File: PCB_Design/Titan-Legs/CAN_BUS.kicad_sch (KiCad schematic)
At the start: 4 parts, among them P2 282837-2, U3 SN65HVD230DR

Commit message: Added high voltage copper fills
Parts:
- R13: footprint Resistor_SMD:R_0603_1608Metric -> Resistor_SMD:R_0402_1005Metric
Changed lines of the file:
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@@
       (effects (font (size 1 1)) (justify left))
     )
-    (property "Footprint" "Resistor_SMD:R_0603_1608Metric" (id 2) (at 108.712 102.87 90)
+    (property "Footprint" "Resistor_SMD:R_0402_1005Metric" (id 2) (at 108.712 102.87 90)
       (effects (font (size 1.27 1.27)) hide)
     )

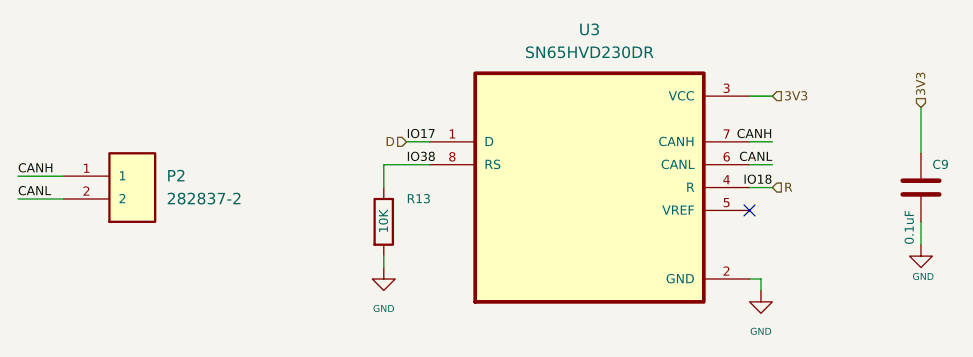
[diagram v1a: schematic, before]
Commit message: Added DRV8323RS Traces and some minor changes
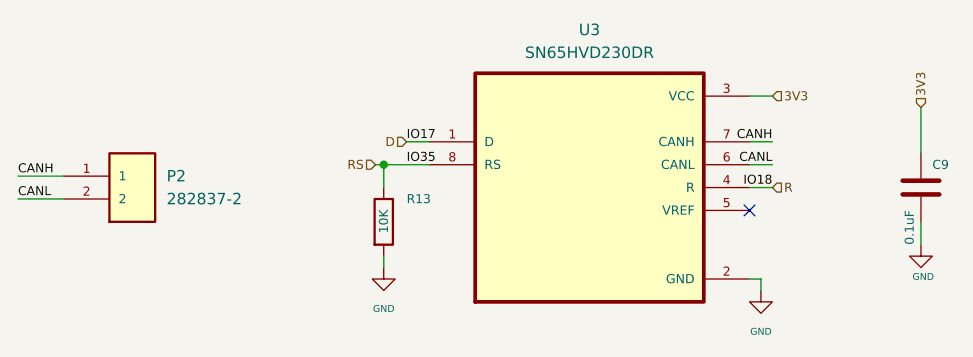
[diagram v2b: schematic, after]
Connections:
- net IO38 renamed RS
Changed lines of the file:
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@@
 (kicad_sch (version 20211123) (generator eeschema)
   (paper "A4")
+  (junction (at 110.49 96.52) (diameter 0) (color 0 0 0 0)
+  )
   (no_connect (at 151.13 101.6))
   (wire (pts (xy 170.18 90.17) (xy 170.18 95.25))
     (stroke (width 0) (type default) (color 0 0 0 0))
   )
-  (wire (pts (xy 110.49 96.52) (xy 115.57 96.52))
+  (wire (pts (xy 109.5756 96.52) (xy 110.49 96.52))
     (stroke (width 0) (type default) (color 0 0 0 0))
   )
@@
     (stroke (width 0) (type default) (color 0 0 0 0))
   )
+  (wire (pts (xy 110.49 96.52) (xy 115.57 96.52))
+    (stroke (width 0) (type default) (color 0 0 0 0))
+  )
   (wire (pts (xy 152.4 109.22) (xy 152.4 110.49))
     (stroke (width 0) (type default) (color 0 0 0 0))
@@
     (effects (font (size 1 1)) (justify right bottom))
   )
-  (label "IO38" (at 113.03 96.52 0)
+  (label "IO35" (at 113.03 96.52 0)
     (effects (font (size 1 1)) (justify left bottom))
   )
@@
     (effects (font (size 1 1)) (justify left))
   )
+  (hierarchical_label "RS" (shape input) (at 109.5756 96.52 180)
+    (effects (font (size 1 1)) (justify right))
+  )
   (symbol (lib_id "power:GND") (at 170.18 105.41 0) (unit 1)
